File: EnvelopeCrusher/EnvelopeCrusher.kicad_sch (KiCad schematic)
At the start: 2 parts

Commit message: updated signal path
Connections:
- net InputFilter/IN is gone; now on net AudioPathSwitching/AUDIO_IN: J_IN1.2 (Pin_2)
- net OutputBuffer/OUT is gone; now on net AudioPathSwitching/AUDIO_OUT: J_OUT1.2 (Pin_2)
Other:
- moved on the sheet: J_IN1, J_OUT1

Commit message: Add routing
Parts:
- added SW?: SW_SPDT, symbol Switch:SW_SPDT
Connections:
- new net AnalogSwitch Sheet/1E: SW?.1 (A)
- new net AnalogSwitch Sheet/2E: SW?.3 (C)
- new net MicroController/CLOCK2: SW?.2 (B)
- no-connect marks 0 -> 1
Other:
- sheet InputFilter renamed InputBuffer
- added sheet AnalogSwitch Sheet (AnalogSwitch.kicad_sch)
- sheet InputBuffer: file InputFilter.kicad_sch -> Buffer.kicad_sch
- sheet InputBuffer ports: added CRUSH_Y, CRUSH_Z, DIRECT_OUT; removed none
- sheet MicroController ports: added CLOCK1, CLOCK2, EnvelopeGen1, EnvelopeGen2, PEAK_IN1; removed none
- sheet OutputBuffer: file untitled.kicad_sch -> Buffer.kicad_sch
- sheet OutputBuffer ports: added CRUSH_Y, CRUSH_Z, DIRECT_OUT; removed none
- sheet StateVariableFilter ports: added SWEEP_3Y, SWEEP_3Z, SWEEP_4Y, SWEEP_4Z; removed none

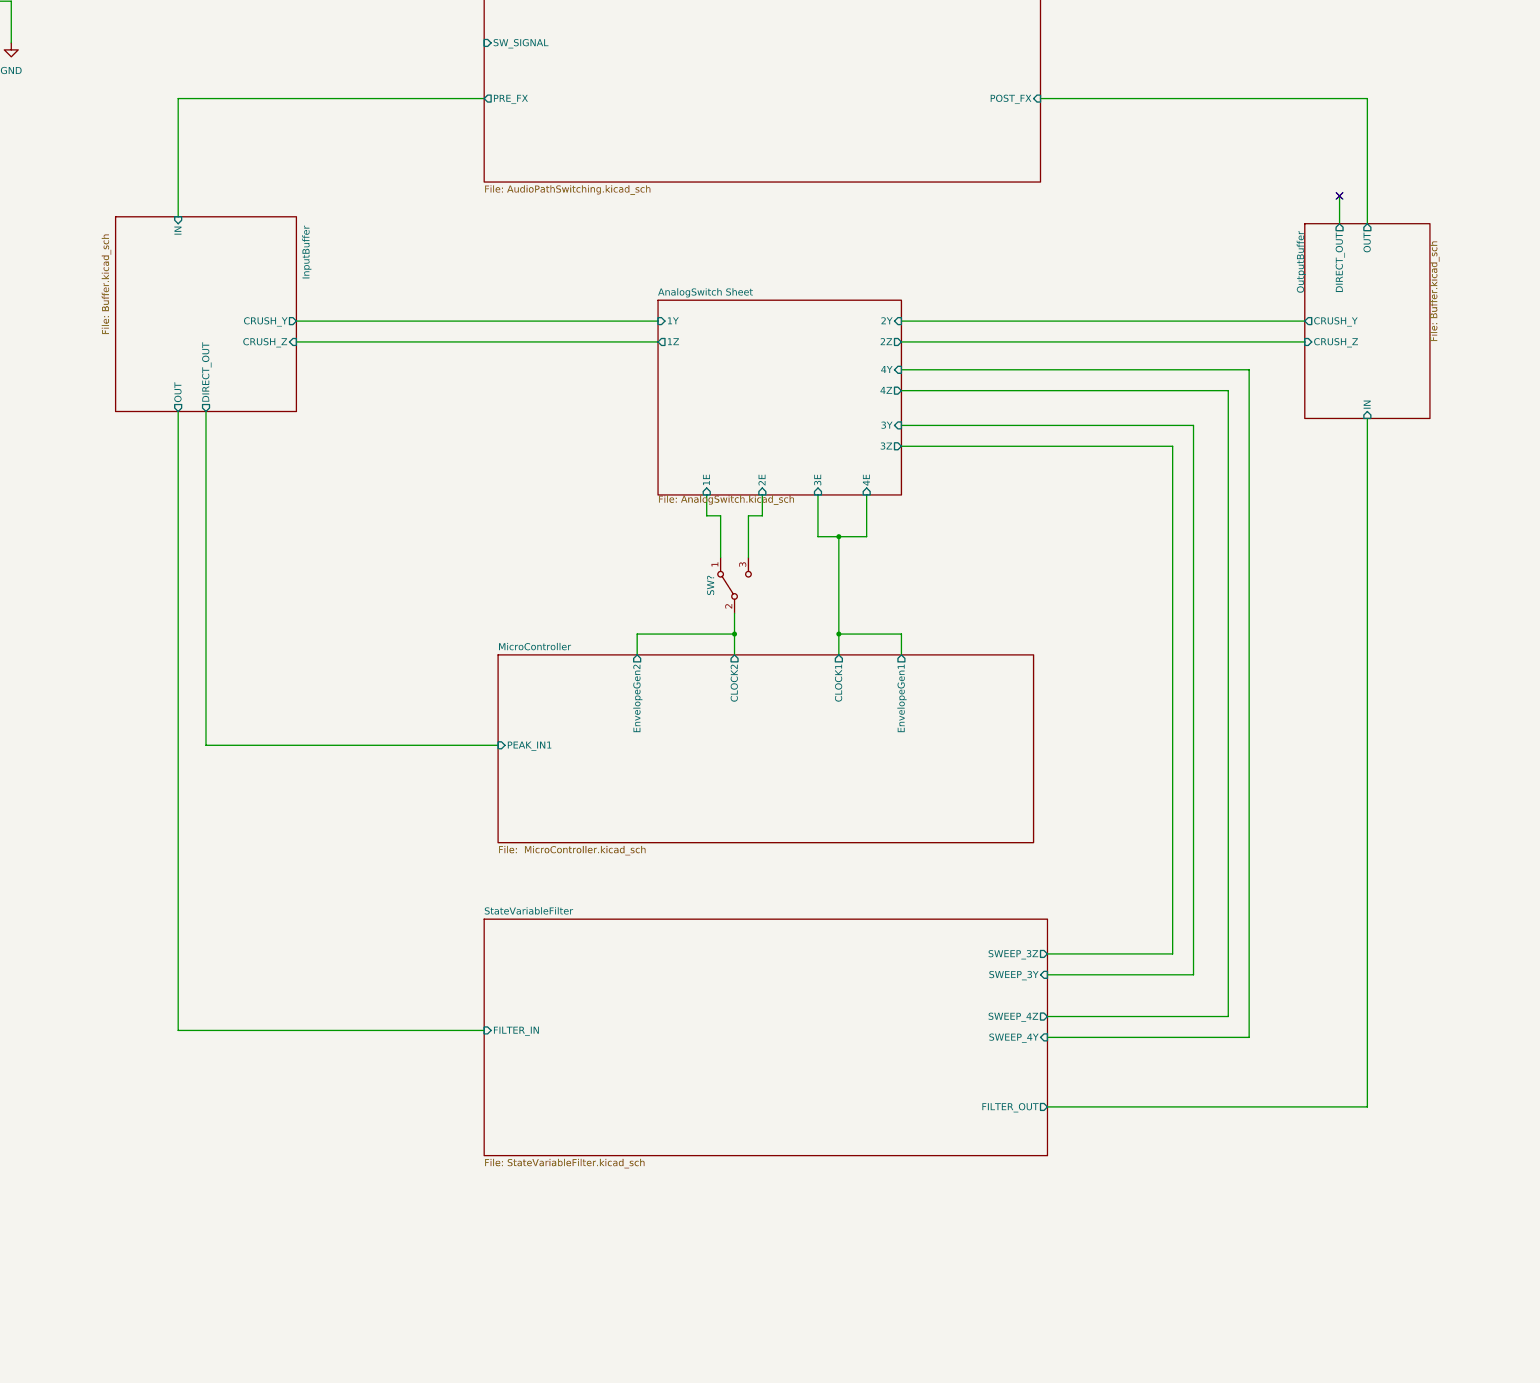
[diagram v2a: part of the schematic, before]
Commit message: REARRANGED BLOCK DIAGRAM AND ROUTING
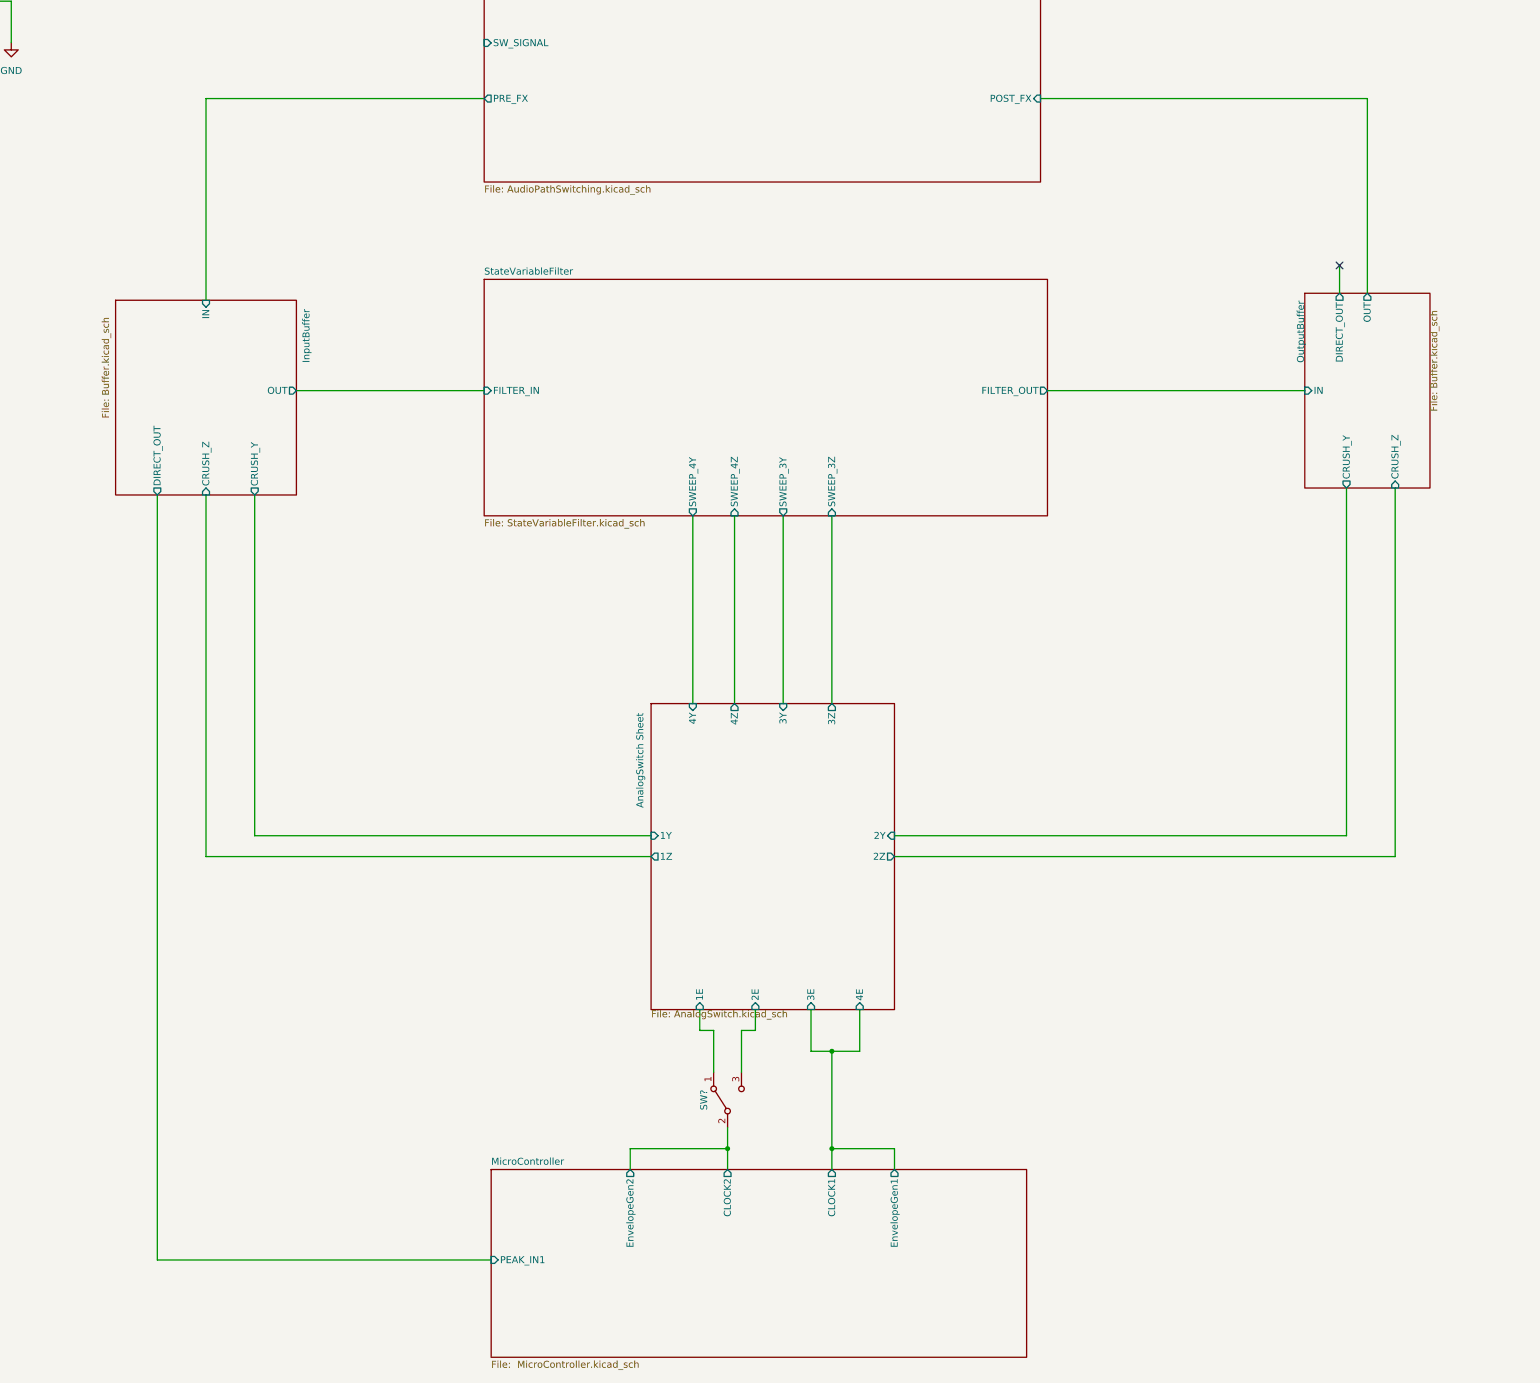
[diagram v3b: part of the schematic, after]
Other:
- moved on the sheet: SW?

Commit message: updated
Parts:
- gave numbers to parts that had none: 1
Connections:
- net MicroController/CLOCK2 renamed MicroController/ENV_CLK_MIX1
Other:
- sheet AnalogSwitch Sheet renamed AnalogSwitch
- sheet AudioPathSwitching ports: added RELAY_SIGNAL; removed SW_SIGNAL
- sheet MicroController ports: added ENV_CLK_MIX1, ENV_CLK_MIX2, RELAY_SIGNAL; removed CLOCK1, CLOCK2, EnvelopeGen1, EnvelopeGen2
- note added: "Pre or Post BitCrusher Select"
- moved on the sheet: SW1
